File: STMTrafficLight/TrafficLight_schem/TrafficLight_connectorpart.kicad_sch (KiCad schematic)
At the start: 7 parts, among them P1 Conn_01x25, P2 Conn_01x25, P3 Conn_01x25, P4 Conn_01x25, U4 LM1117MP-3.3

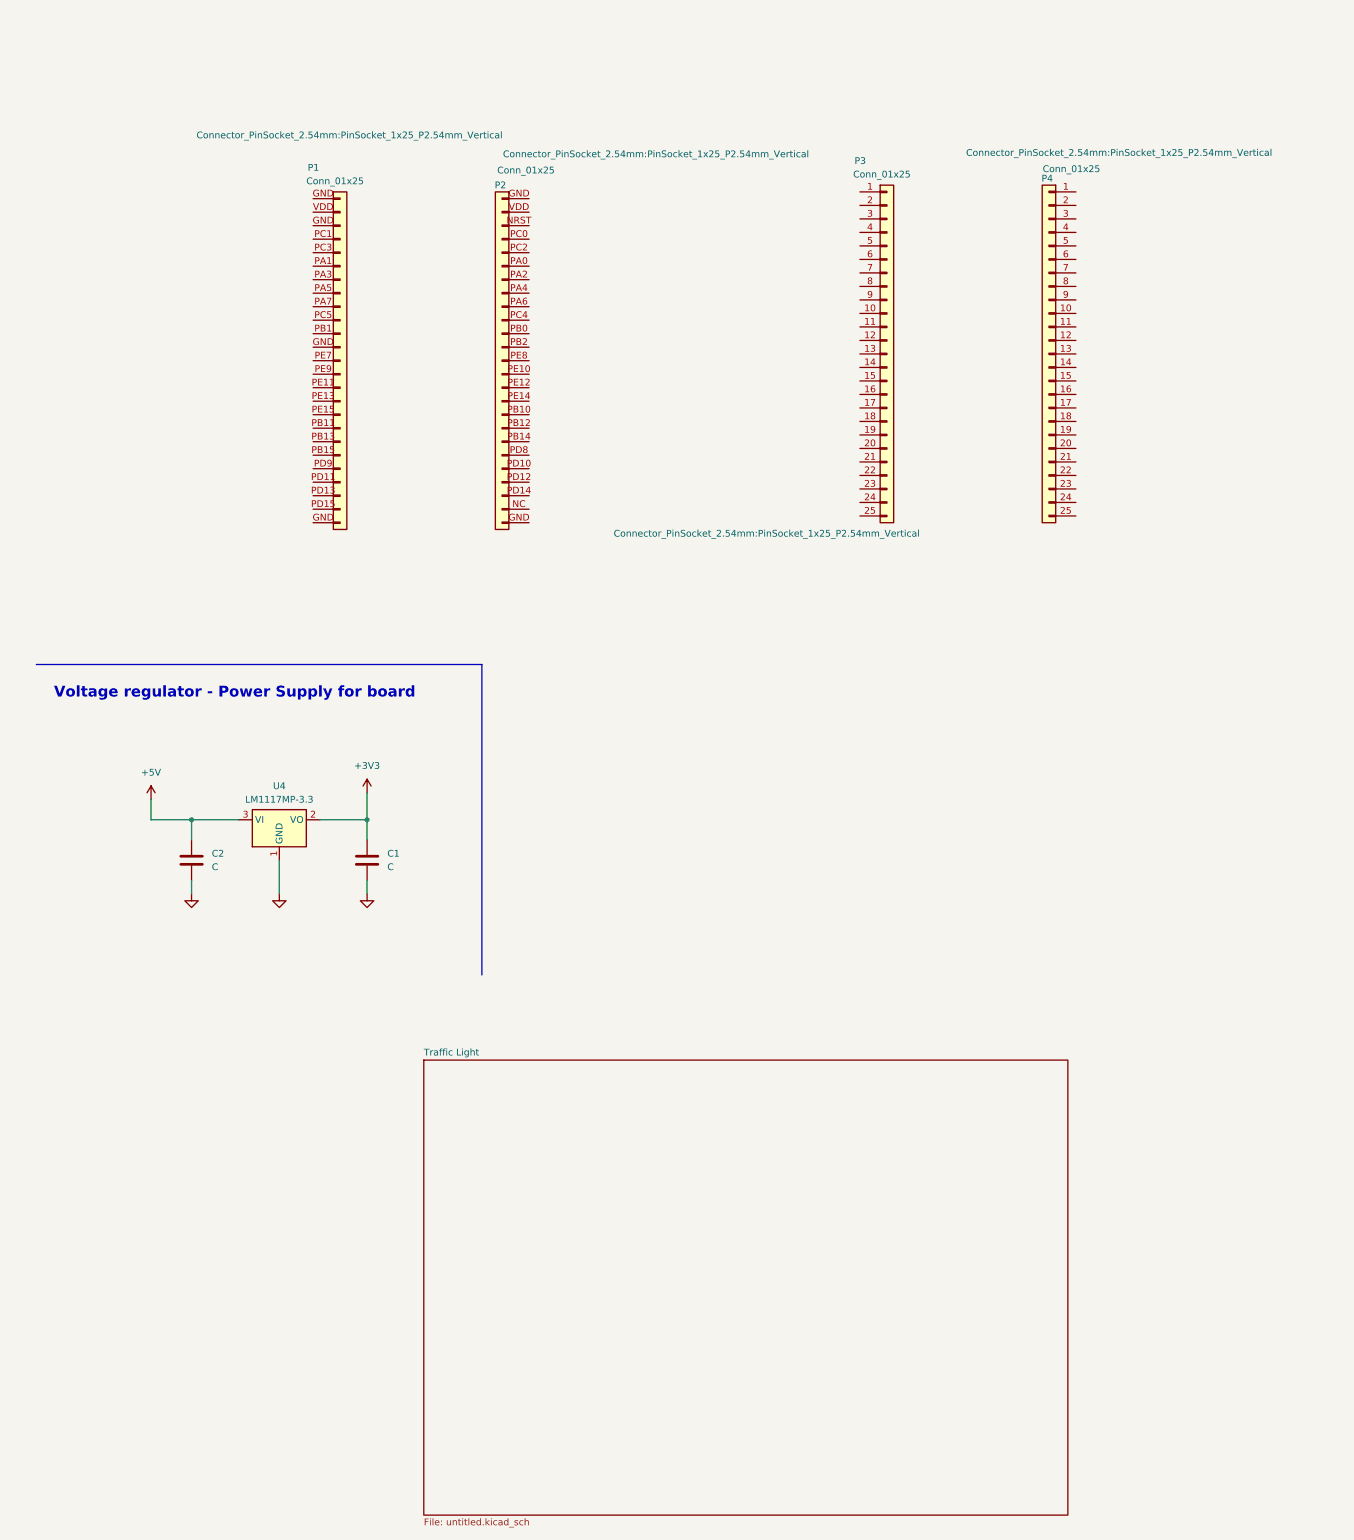
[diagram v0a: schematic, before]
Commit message: Marked connectors and added power LEDs, fixed resistors
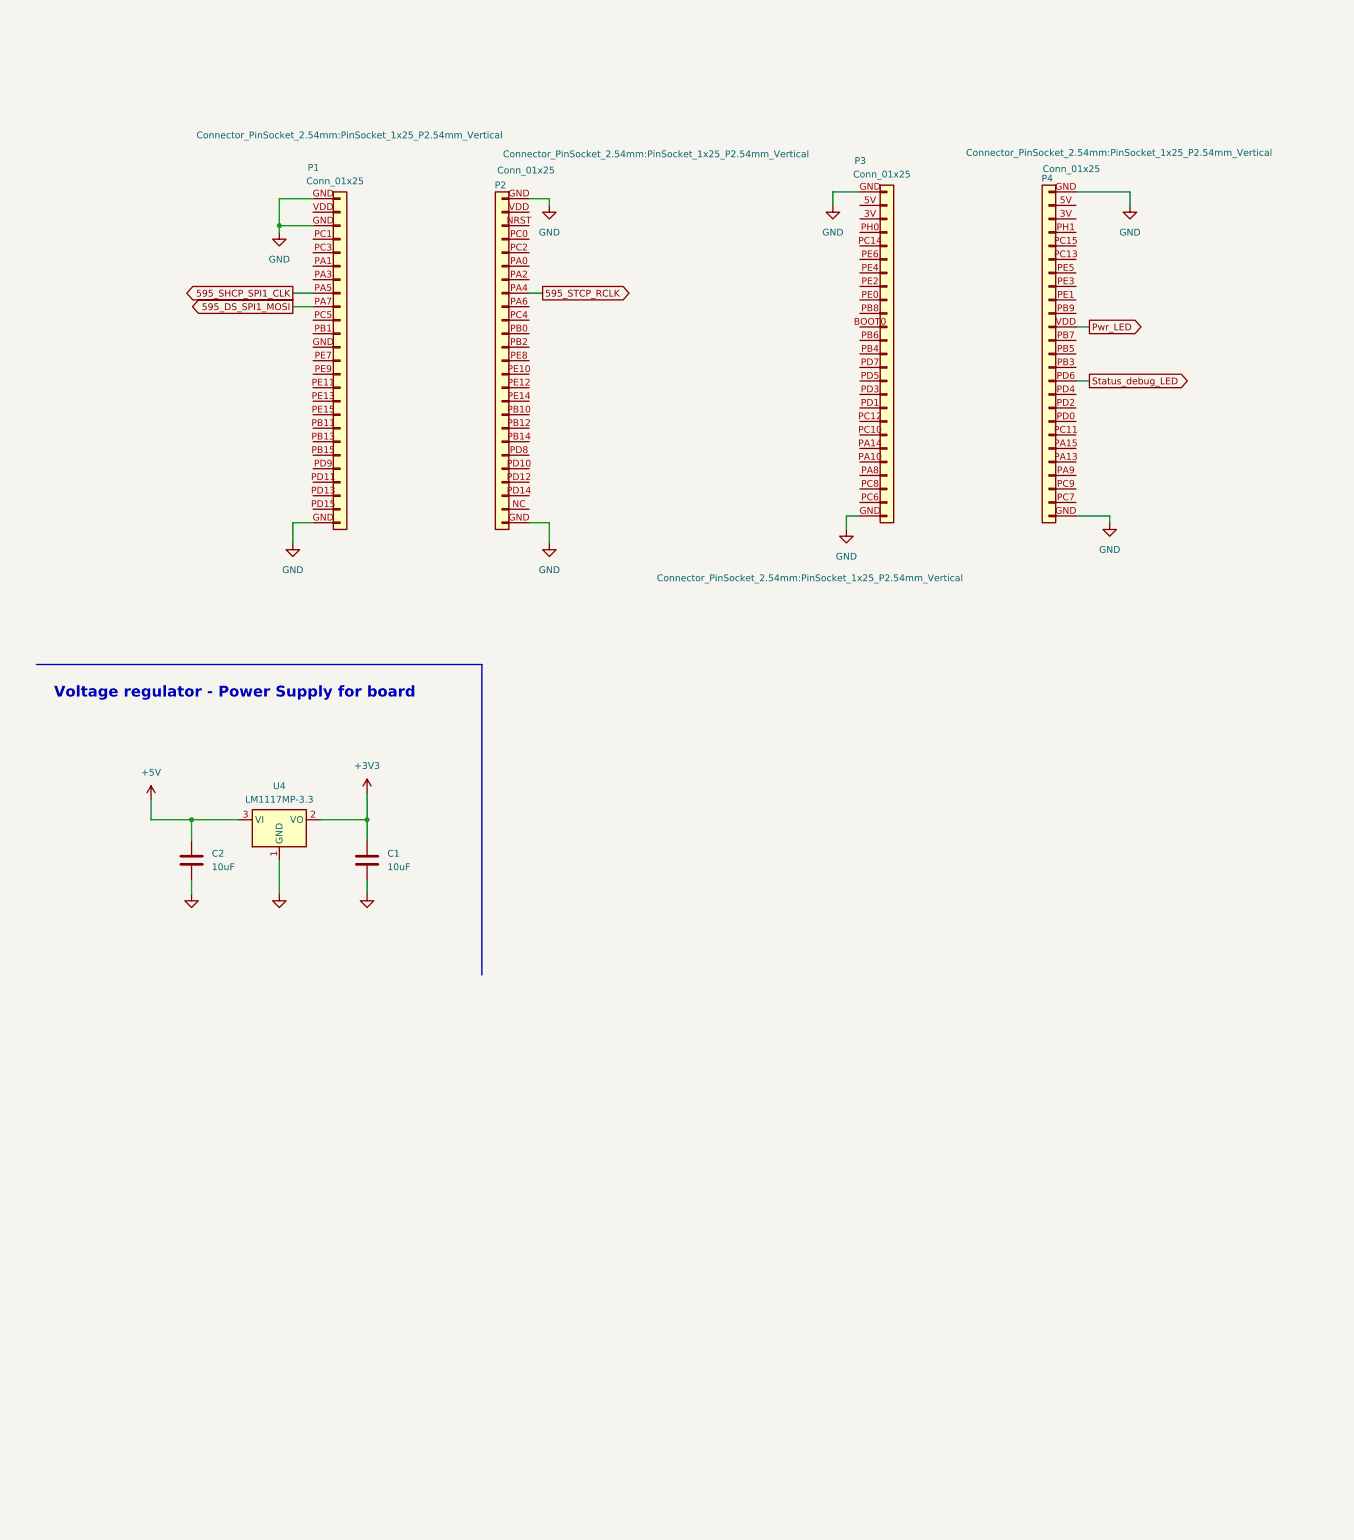
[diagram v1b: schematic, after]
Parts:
- C1, C2: value C -> 10uF
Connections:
- net GND: now also P1.GND, P2.GND (Pin_25), P3.GND (Pin_25), P4.GND (Pin_25)
- net 595_STCP_RCLK: now reaches P2.PA4 (Pin_8)
- net 595_SHCP_SPI1_CLK: now reaches P1.PA5
- net 595_DS_SPI1_MOSI: now reaches P1.PA7
- new net Pwr_LED: P4.VDD (Pin_11)
- new net Status_debug_LED: P4.PD6 (Pin_15)
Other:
- removed sheet Traffic Light
- moved on the sheet: P3

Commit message: Marked connectors and added power LEDs, fixed resistors
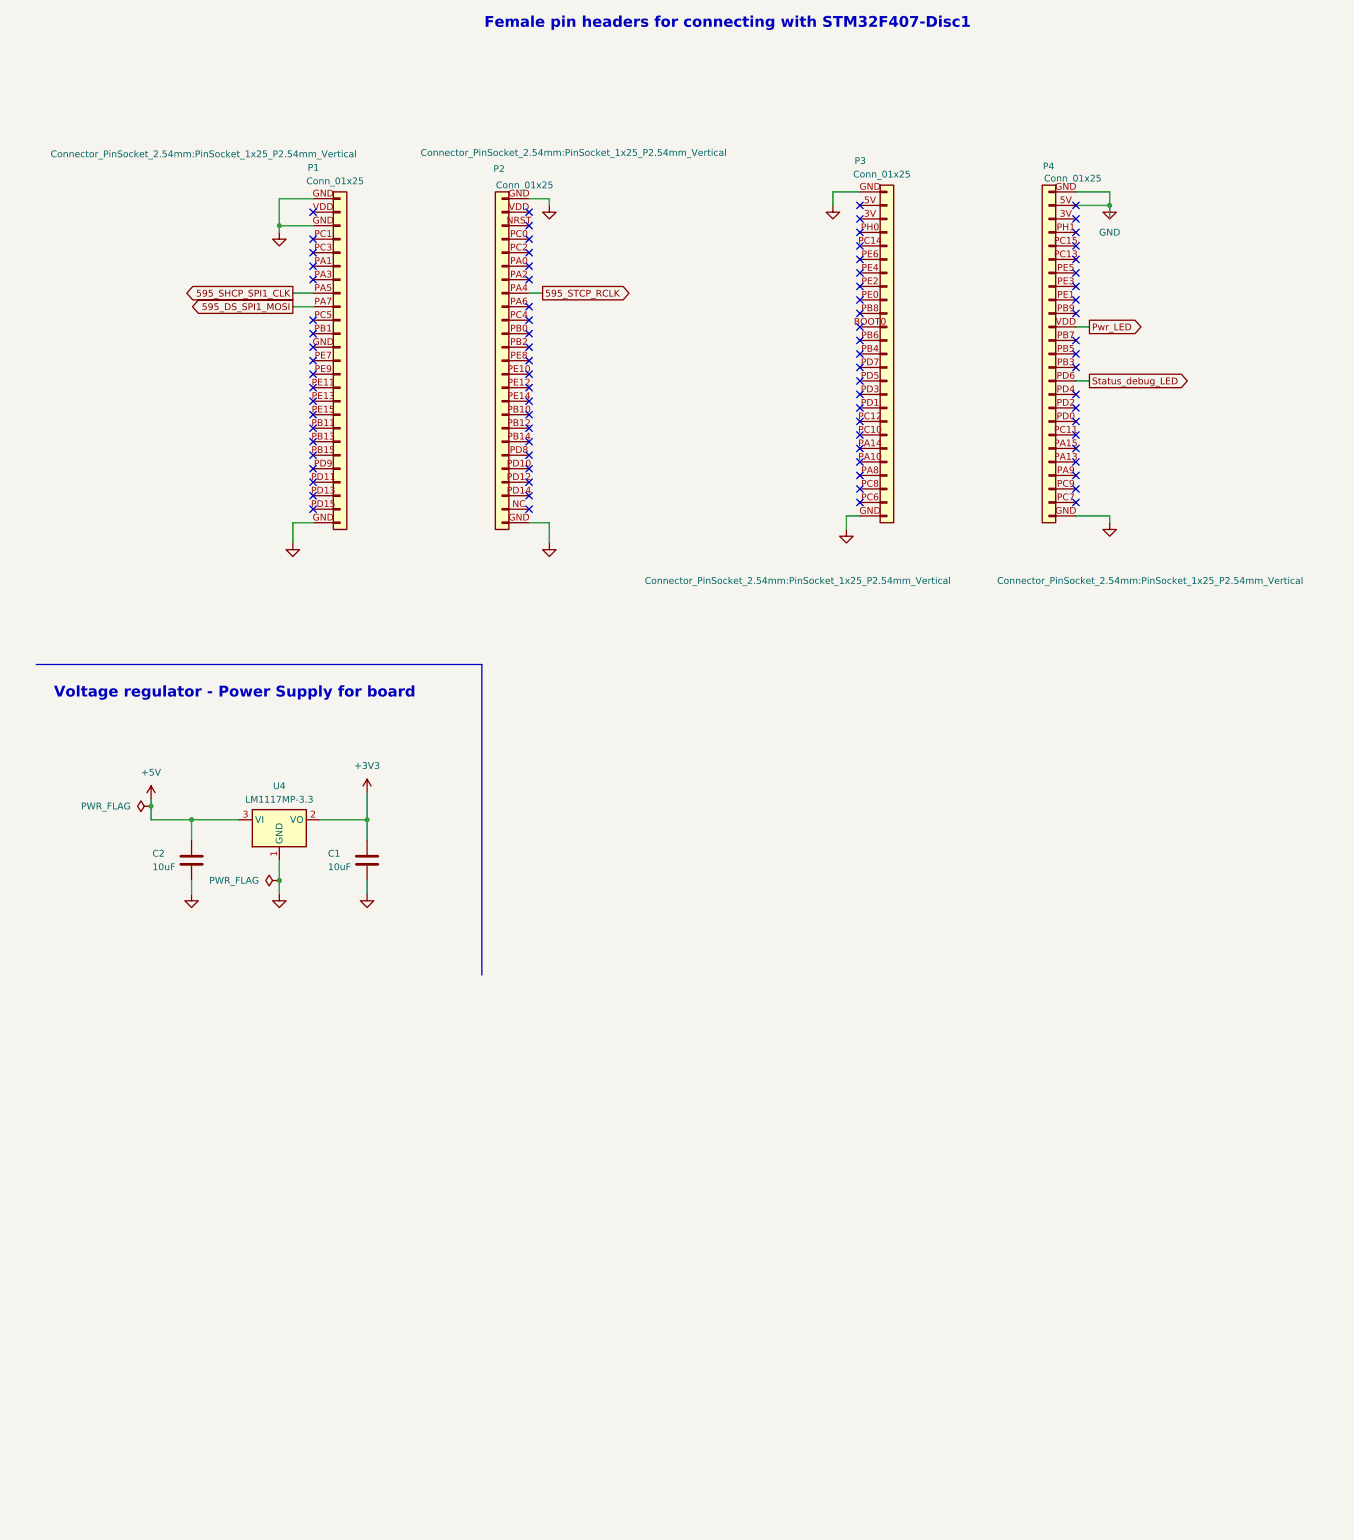
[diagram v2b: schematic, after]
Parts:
- C1, C2: footprint (none) -> Capacitor_SMD:C_0603_1608Metric; Distributor link 1 (none) -> https://eu.mouser.com/ProductDetail/Samsung-Electro-Mechani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; Distributor link 2 (none) -> https://www.digikey.com/en/products/detail/samsung-electro-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; LCSC (none) -> C19702; Manufacturer (none) -> Samsung Electro-Mechanics; Manufacturer part number (none) -> CL10A106KP8NNNC
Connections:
- net GND: now also P4.5V (Pin_2)
- no-connect marks 0 -> 86
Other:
- note added: "Female pin headers for connecting with STM32F407-Disc1"

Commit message: Finally started the PCB design
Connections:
- net +5V: now also P3.5V (Pin_2), P4.5V (Pin_2)
- net GND: no longer P4.5V (Pin_2)
- net +3.3V: now reaches P3.3V (Pin_3)
- net +3.3V: now also P4.3V (Pin_3)
- net PL2_Switch: now reaches P3.PC8 (Pin_23)
- net TL2_Car: now reaches P2.PB0
- net PL1_Switch: now reaches P2.PD10
- net TL4_Car: now reaches P4.PA15 (Pin_20)
- net TL3_Car: now reaches P4.PD0 (Pin_18)
- net TL1_Car: now reaches P1.PD13
- no-connect marks 86 -> 76
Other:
- added sheet TrafficLight_lightpart (TrafficLight_lightpart.kicad_sch)
